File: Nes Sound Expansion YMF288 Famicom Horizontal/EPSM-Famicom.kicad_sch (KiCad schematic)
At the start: 59 parts, among them J1 CARTRIDGE_F, J2 OUT_1, J3 EPSM_ADDRESSING, J4 CONSOLE_M, J5 AudioJack4_SwitchTR1, U1 74LS174, U10 74LS257, U2 74LS174, U3 74LS139, U4 74LS132, U5 YMF288, U6 BU9480F, U7 74LS257, U8 74LS257, U9 LM358, X1 SG-8002CA

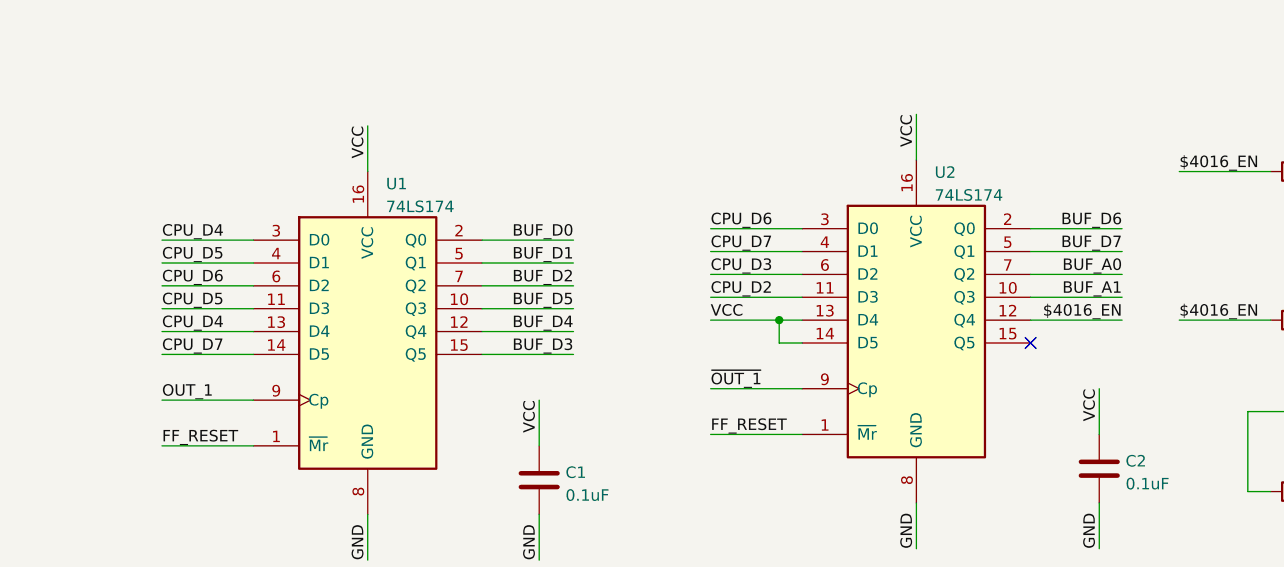
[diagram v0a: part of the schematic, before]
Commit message: Fix erroneous $4016 data latch lines
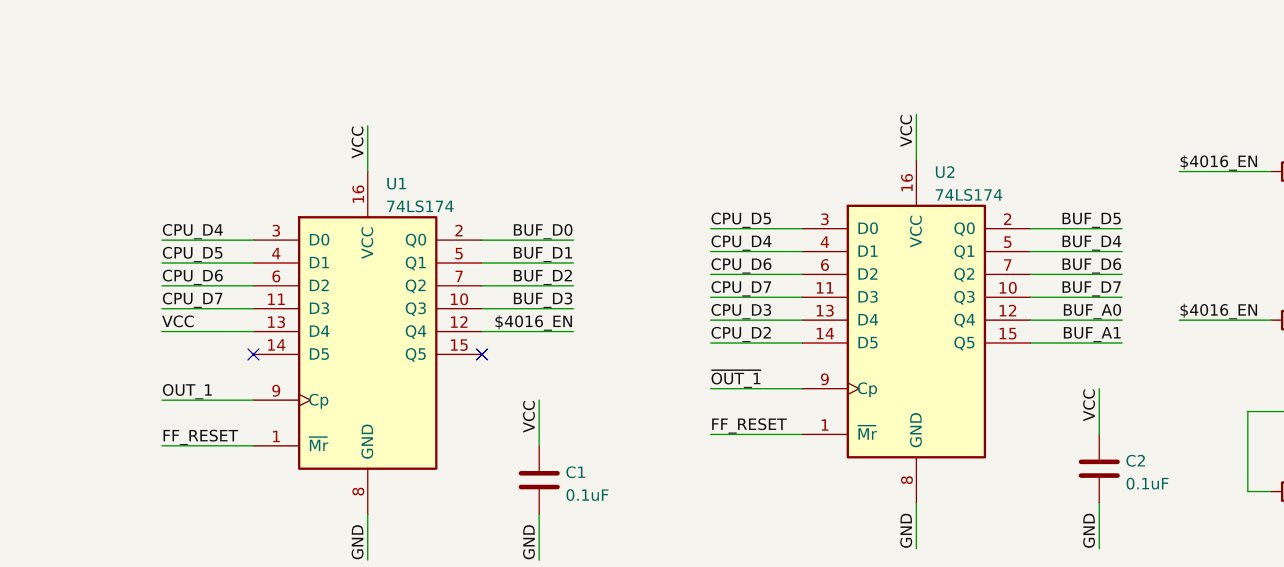
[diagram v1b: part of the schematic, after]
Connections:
- net $4016_EN: now also U1.12 (Q4); no longer U2.12 (Q4)
- net BUF_A0: now also U2.12 (Q4); no longer U2.7 (Q2)
- net BUF_A1: now also U2.15 (Q5); no longer U2.10 (Q3)
- net BUF_D3: now also U1.10 (Q3); no longer U1.15 (Q5)
- net BUF_D4: now also U2.5 (Q1); no longer U1.12 (Q4)
- net BUF_D5: now also U2.2 (Q0); no longer U1.10 (Q3)
- net BUF_D6: now also U2.7 (Q2); no longer U2.2 (Q0)
- net BUF_D7: now also U2.10 (Q3); no longer U2.5 (Q1)
- net CPU_D2: now also U2.14 (D5); no longer U2.11 (D3)
- net CPU_D3: now also U2.13 (D4); no longer U2.6 (D2)
- net CPU_D4: now also U2.4 (D1); no longer U1.13 (D4)
- net CPU_D5: now also U2.3 (D0); no longer U1.11 (D3)
- net CPU_D6: now also U2.6 (D2); no longer U2.3 (D0)
- net CPU_D7: now also U1.11 (D3), U2.11 (D3); no longer U1.14 (D5), U2.4 (D1)
- net VCC: now also U1.13 (D4); no longer U2.13 (D4), U2.14 (D5)
- no-connect marks 16 -> 17

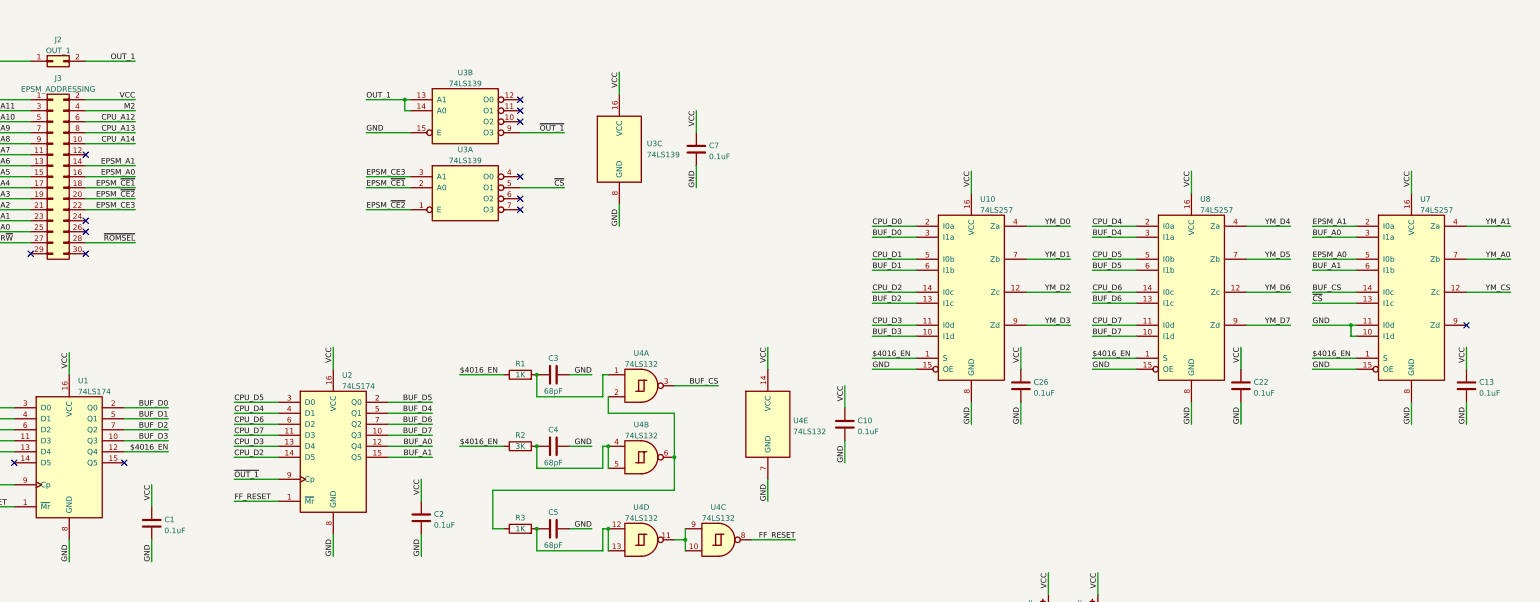
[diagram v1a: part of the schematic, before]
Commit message: Fix footprint size errors
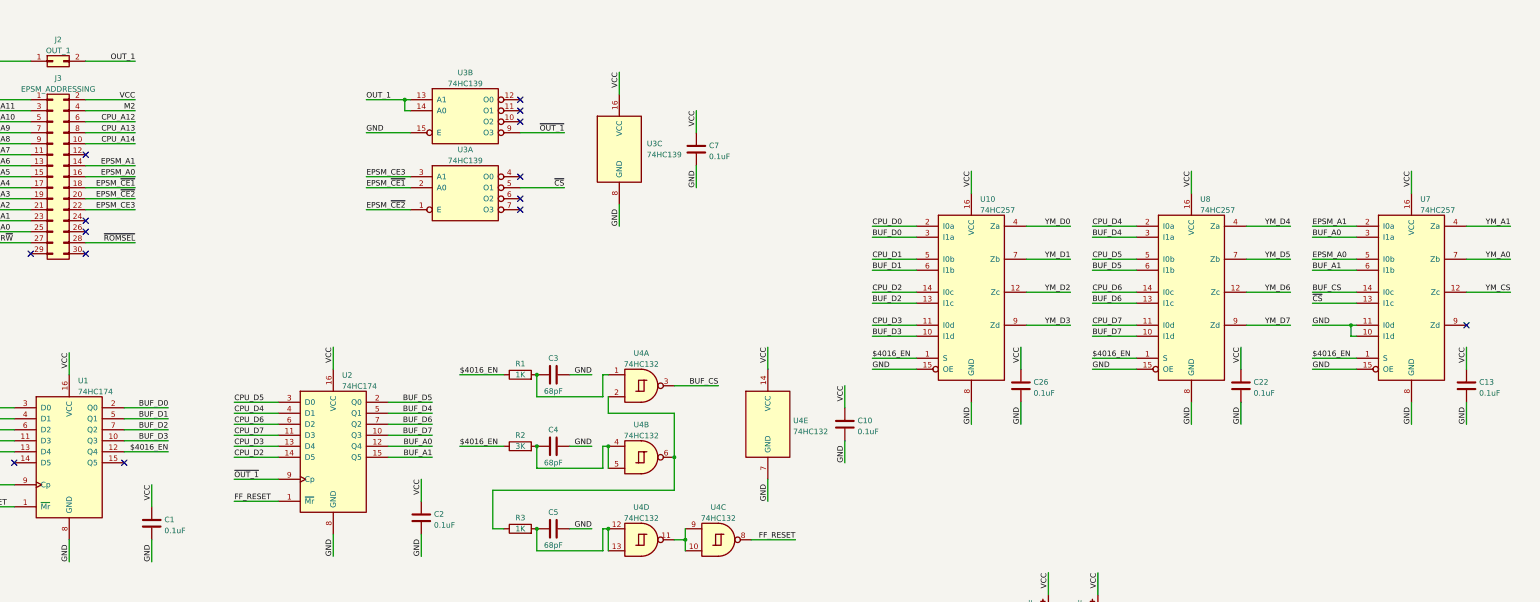
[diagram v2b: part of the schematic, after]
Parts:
- U1, U2: value 74LS174 -> 74HC174
- U10, U7, U8: value 74LS257 -> 74HC257
- U3: value 74LS139 -> 74HC139
- U4: value 74LS132 -> 74HC132
- U5: footprint EPSM-Famicom:SOP-28_7.5x12.8mm_P1.27mm -> EPSM-Famicom:SOP-28_8.4x18.1mm_P1.27mm
- U6: footprint Package_SO:SOIC-8_5.275x5.275mm_P1.27mm -> Package_SO:SOIC-8_3.9x4.9mm_P1.27mm
- X1: footprint Oscillator:Oscillator_SMD_SeikoEpson_SG8002LB-4Pin_5.0x3.2mm -> Oscillator:Oscillator_SMD_Abracon_ASV-4Pin_7.0x5.1mm
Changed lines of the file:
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@@
       (effects (font (size 1.27 1.27)) (justify left))
     )
-    (property "Footprint" "EPSM-Famicom:SOP-28_7.5x12.8mm_P1.27mm" (id 2) (at 195.58 81.28 0)
-      (effects (font (size 1.27 1.27)) hide)
-    )
-    (property "Datasheet" "" (id 3) (at 195.58 81.28 0)
+    (property "Footprint" "EPSM-Famicom:SOP-28_8.4x18.1mm_P1.27mm" (id 2) (at 195.58 81.28 0)
+      (effects (font (size 1.27 1.27)) hide)
+    )
+    (property "Datasheet" "https://www.quarter-dev.info/archives/yamaha/YMF288.pdf" (id 3) (at 195.58 81.28 0)
       (effects (font (size 1.27 1.27)) hide)
     )
@@
       (effects (font (size 1.27 1.27)) (justify left))
     )
-    (property "Value" "74LS257" (id 1) (at 258.5594 175.3671 0)
+    (property "Value" "74HC257" (id 1) (at 258.5594 175.3671 0)
       (effects (font (size 1.27 1.27)) (justify left))
     )
@@
       (effects (font (size 1.27 1.27)) (justify left))
     )
-    (property "Value" "74LS174" (id 1) (at 111.2394 216.0071 0)
+    (property "Value" "74HC174" (id 1) (at 111.2394 216.0071 0)
       (effects (font (size 1.27 1.27)) (justify left))
     )
@@
       (effects (font (size 1.27 1.27)) (justify left))
     )
-    (property "Value" "74LS257" (id 1) (at 309.3594 175.3671 0)
+    (property "Value" "74HC257" (id 1) (at 309.3594 175.3671 0)
       (effects (font (size 1.27 1.27)) (justify left))
     )
@@
     (in_bom yes) (on_board yes)
     (property "Reference" "U4" (id 0) (at 180.34 243.9502 0))
-    (property "Value" "74LS132" (id 1) (at 180.34 246.4871 0))
+    (property "Value" "74HC132" (id 1) (at 180.34 246.4871 0))
     (property "Footprint" "Package_SO:SOIC-14_3.9x8.7mm_P1.27mm" (id 2) (at 180.34 251.46 0)
       (effects (font (size 1.27 1.27)) hide)
@@
       (effects (font (size 1.27 1.27)) (justify left))
     )
-    (property "Footprint" "Oscillator:Oscillator_SMD_SeikoEpson_SG8002LB-4Pin_5.0x3.2mm" (id 2) (at 226.06 55.88 0)
+    (property "Footprint" "Oscillator:Oscillator_SMD_Abracon_ASV-4Pin_7.0x5.1mm" (id 2) (at 226.06 55.88 0)
       (effects (font (size 1.27 1.27)) hide)
     )
@@
     (in_bom yes) (on_board yes) (fields_autoplaced)
     (property "Reference" "U3" (id 0) (at 139.7 161.4002 0))
-    (property "Value" "74LS139" (id 1) (at 139.7 163.9371 0))
+    (property "Value" "74HC139" (id 1) (at 139.7 163.9371 0))
     (property "Footprint" "Package_SO:SOIC-16_3.9x9.9mm_P1.27mm" (id 2) (at 139.7 170.18 0)
       (effects (font (size 1.27 1.27)) hide)
@@
     (in_bom yes) (on_board yes) (fields_autoplaced)
     (property "Reference" "U4" (id 0) (at 180.34 224.9002 0))
-    (property "Value" "74LS132" (id 1) (at 180.34 227.4371 0))
+    (property "Value" "74HC132" (id 1) (at 180.34 227.4371 0))
     (property "Footprint" "Package_SO:SOIC-14_3.9x8.7mm_P1.27mm" (id 2) (at 180.34 232.41 0)
       (effects (font (size 1.27 1.27)) hide)
@@
       (effects (font (size 1.27 1.27)) (justify left))
     )
-    (property "Value" "74LS132" (id 1) (at 215.392 226.4922 0)
+    (property "Value" "74HC132" (id 1) (at 215.392 226.4922 0)
       (effects (font (size 1.27 1.27)) (justify left))
     )
@@
     (in_bom yes) (on_board yes) (fields_autoplaced)
     (property "Reference" "U4" (id 0) (at 180.34 208.3902 0))
-    (property "Value" "74LS132" (id 1) (at 180.34 210.9271 0))
+    (property "Value" "74HC132" (id 1) (at 180.34 210.9271 0))
     (property "Footprint" "Package_SO:SOIC-14_3.9x8.7mm_P1.27mm" (id 2) (at 180.34 215.9 0)
       (effects (font (size 1.27 1.27)) hide)
@@
       (effects (font (size 1.27 1.27)) (justify left))
     )
-    (property "Value" "74LS257" (id 1) (at 360.1594 175.3671 0)
+    (property "Value" "74HC257" (id 1) (at 360.1594 175.3671 0)
       (effects (font (size 1.27 1.27)) (justify left))
     )
@@
     (in_bom yes) (on_board yes) (fields_autoplaced)
     (property "Reference" "U3" (id 0) (at 139.7 143.6202 0))
-    (property "Value" "74LS139" (id 1) (at 139.7 146.1571 0))
+    (property "Value" "74HC139" (id 1) (at 139.7 146.1571 0))
     (property "Footprint" "Package_SO:SOIC-16_3.9x9.9mm_P1.27mm" (id 2) (at 139.7 152.4 0)
       (effects (font (size 1.27 1.27)) hide)
@@
     (in_bom yes) (on_board yes) (fields_autoplaced)
     (property "Reference" "U4" (id 0) (at 198.12 243.9502 0))
-    (property "Value" "74LS132" (id 1) (at 198.12 246.4871 0))
+    (property "Value" "74HC132" (id 1) (at 198.12 246.4871 0))
     (property "Footprint" "Package_SO:SOIC-14_3.9x8.7mm_P1.27mm" (id 2) (at 198.12 251.46 0)
       (effects (font (size 1.27 1.27)) hide)
@@
       (effects (font (size 1.27 1.27)) (justify left))
     )
-    (property "Value" "74LS139" (id 1) (at 181.61 162.56 0)
+    (property "Value" "74HC139" (id 1) (at 181.61 162.56 0)
       (effects (font (size 1.27 1.27)) (justify left))
     )
@@
       (effects (font (size 1.27 1.27)) (justify left))
     )
-    (property "Footprint" "Package_SO:SOIC-8_5.275x5.275mm_P1.27mm" (id 2) (at 233.68 74.93 0)
+    (property "Footprint" "Package_SO:SOIC-8_3.9x4.9mm_P1.27mm" (id 2) (at 233.68 74.93 0)
       (effects (font (size 1.27 1.27)) hide)
     )
@@
       (effects (font (size 1.27 1.27)) (justify left))
     )
-    (property "Value" "74LS174" (id 1) (at 50.2794 217.2771 0)
+    (property "Value" "74HC174" (id 1) (at 50.2794 217.2771 0)
       (effects (font (size 1.27 1.27)) (justify left))
     )
@@
     )
     (path "/ffa9b3d0-5a2b-4008-a1d1-ba0783fbcd78"
-      (reference "U1") (unit 1) (value "74LS174") (footprint "Package_SO:SOIC-16_3.9x9.9mm_P1.27mm")
+      (reference "U1") (unit 1) (value "74HC174") (footprint "Package_SO:SOIC-16_3.9x9.9mm_P1.27mm")
     )
     (path "/0a512736-9db6-4093-98c5-8298b2002bd9"
-      (reference "U2") (unit 1) (value "74LS174") (footprint "Package_SO:SOIC-16_3.9x9.9mm_P1.27mm")
+      (reference "U2") (unit 1) (value "74HC174") (footprint "Package_SO:SOIC-16_3.9x9.9mm_P1.27mm")
     )
     (path "/48d1e52a-2236-4c12-94d5-ffccc100ea49"
-      (reference "U3") (unit 1) (value "74LS139") (footprint "Package_SO:SOIC-16_3.9x9.9mm_P1.27mm")
+      (reference "U3") (unit 1) (value "74HC139") (footprint "Package_SO:SOIC-16_3.9x9.9mm_P1.27mm")
     )
     (path "/94ff7ccf-1795-4c28-b581-f2ea7c835610"
-      (reference "U3") (unit 2) (value "74LS139") (footprint "Package_SO:SOIC-16_3.9x9.9mm_P1.27mm")
+      (reference "U3") (unit 2) (value "74HC139") (footprint "Package_SO:SOIC-16_3.9x9.9mm_P1.27mm")
     )
     (path "/c0c18a2a-6376-4fa0-9928-c3b0ce3e0e91"
-      (reference "U3") (unit 3) (value "74LS139") (footprint "Package_SO:SOIC-16_3.9x9.9mm_P1.27mm")
+      (reference "U3") (unit 3) (value "74HC139") (footprint "Package_SO:SOIC-16_3.9x9.9mm_P1.27mm")
     )
     (path "/83ed3325-163c-4afa-93c5-49baeb4cd081"
-      (reference "U4") (unit 1) (value "74LS132") (footprint "Package_SO:SOIC-14_3.9x8.7mm_P1.27mm")
+      (reference "U4") (unit 1) (value "74HC132") (footprint "Package_SO:SOIC-14_3.9x8.7mm_P1.27mm")
     )
     (path "/599fbcfe-5e39-4f5e-8245-7a38ebea64d1"
-      (reference "U4") (unit 2) (value "74LS132") (footprint "Package_SO:SOIC-14_3.9x8.7mm_P1.27mm")
+      (reference "U4") (unit 2) (value "74HC132") (footprint "Package_SO:SOIC-14_3.9x8.7mm_P1.27mm")
     )
     (path "/a010cd21-0c47-4838-97cf-f6952c9f247c"
-      (reference "U4") (unit 3) (value "74LS132") (footprint "Package_SO:SOIC-14_3.9x8.7mm_P1.27mm")
+      (reference "U4") (unit 3) (value "74HC132") (footprint "Package_SO:SOIC-14_3.9x8.7mm_P1.27mm")
     )
     (path "/2d006010-ba6c-4126-adf6-9df43d863282"
-      (reference "U4") (unit 4) (value "74LS132") (footprint "Package_SO:SOIC-14_3.9x8.7mm_P1.27mm")
+      (reference "U4") (unit 4) (value "74HC132") (footprint "Package_SO:SOIC-14_3.9x8.7mm_P1.27mm")
     )
     (path "/789ef0a4-200d-4a4a-b78e-3e6610a4c3b8"
-      (reference "U4") (unit 5) (value "74LS132") (footprint "Package_SO:SOIC-14_3.9x8.7mm_P1.27mm")
+      (reference "U4") (unit 5) (value "74HC132") (footprint "Package_SO:SOIC-14_3.9x8.7mm_P1.27mm")
     )
     (path "/04721b2a-b8fe-4628-b3cc-831c2dbc8b4f"
-      (reference "U5") (unit 1) (value "YMF288") (footprint "EPSM-Famicom:SOP-28_7.5x12.8mm_P1.27mm")
+      (reference "U5") (unit 1) (value "YMF288") (footprint "EPSM-Famicom:SOP-28_8.4x18.1mm_P1.27mm")
     )
     (path "/d02f9b5f-57b8-4b22-ba74-372e25af5469"
-      (reference "U6") (unit 1) (value "BU9480F") (footprint "Package_SO:SOIC-8_5.275x5.275mm_P1.27mm")
+      (reference "U6") (unit 1) (value "BU9480F") (footprint "Package_SO:SOIC-8_3.9x4.9mm_P1.27mm")
     )
     (path "/91bb666c-cdad-4b85-b6b9-1567d0f51104"
-      (reference "U7") (unit 1) (value "74LS257") (footprint "Package_SO:SOIC-16_3.9x9.9mm_P1.27mm")
+      (reference "U7") (unit 1) (value "74HC257") (footprint "Package_SO:SOIC-16_3.9x9.9mm_P1.27mm")
     )
     (path "/13e2216a-5685-44fb-b37b-e3377d494a4d"
-      (reference "U8") (unit 1) (value "74LS257") (footprint "Package_SO:SOIC-16_3.9x9.9mm_P1.27mm")
+      (reference "U8") (unit 1) (value "74HC257") (footprint "Package_SO:SOIC-16_3.9x9.9mm_P1.27mm")
     )
     (path "/387d75e5-30ff-4e24-b0ee-c5bf67a456b6"
@@
     )
     (path "/07e9be1b-d34d-4a14-ad60-a9f8f1ba9a04"
-      (reference "U10") (unit 1) (value "74LS257") (footprint "Package_SO:SOIC-16_3.9x9.9mm_P1.27mm")
+      (reference "U10") (unit 1) (value "74HC257") (footprint "Package_SO:SOIC-16_3.9x9.9mm_P1.27mm")
     )
     (path "/487fe2b3-0e38-4935-9823-96c09d72da99"
-      (reference "X1") (unit 1) (value "SG-8002CA") (footprint "Oscillator:Oscillator_SMD_SeikoEpson_SG8002LB-4Pin_5.0x3.2mm")
-    )
-  )
+      (reference "X1") (unit 1) (value "SG-8002CA") (footprint "Oscillator:Oscillator_SMD_Abracon_ASV-4Pin_7.0x5.1mm")
+    )
+  )

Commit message: Remove daughterboard connector; use two layers
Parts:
- removed C14, C15: 100uF, Capacitor_THT:CP_Radial_D5.0mm_P2.50mm, symbol Device:C_Polarized
- removed J2: OUT_1, Connector_PinHeader_2.54mm:PinHeader_1x02_P2.54mm_Vertical, symbol Connector_Generic:Conn_02x01
- removed J3: EPSM_ADDRESSING, Connector_PinSocket_2.54mm:PinSocket_2x15_P2.54mm_Vertical_SMD, symbol Connector_Generic:Conn_02x15_Odd_Even
- added C1, C10, C21, C30, C4: 0.1uF, Capacitor_SMD:C_0805_2012Metric_Pad1.18x1.45mm_HandSolder, symbol Device:C
- added C16, C18: 100uF, Capacitor_SMD:CP_Elec_6.3x5.4, symbol Device:C_Polarized
- added U1, U5, U6: 74HC688, Package_SO:SOIC-20W_7.5x12.8mm_P1.27mm, symbol 74xx:74HC688
- added U10: 74HC132, Package_SO:SOIC-14_3.9x8.7mm_P1.27mm, symbol 74xx:74LS132
- added U14: 74LVC1G373, Package_TO_SOT_SMD:SOT-23-6, symbol 74xGxx:74LVC1G373
- renumbered C8 to C11, C10 to C12, C9 to C13, C11 to C14, C12 to C15, C26 to C17, C16 to C19, C1 to C2, C17 to C20, C18 to C22, C19 to C23, C20 to C24, C21 to C25, C22 to C26, C23 to C27, C24 to C28, C25 to C29, C7 to C3, C13 to C31, C2 to C5, C3 to C6, C4 to C7, C5 to C8, C6 to C9, J4 to J2, J5 to J3, U10 to U11, U8 to U12, U9 to U13, U7 to U15, U3 to U2, U1 to U3, U2 to U4, U4 to U7, U5 to U8, U6 to U9
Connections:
- net EPSM_CE3 is gone; now on net VCC: U2.3 (A1)
- net EPSM_~{CE1} is gone; now on net GND: U2.2 (A0)
- net $4016_EN: now also U3.7 (Q2); no longer U3.12 (Q4)
- net BUF_A0: now also U4.7 (Q2); no longer U4.12 (Q4)
- net BUF_A1: now also U15.13 (I1c), U4.10 (Q3); no longer U15.6 (I1b), U4.15 (Q5)
- net BUF_CS: now also U15.5 (I0b); no longer U15.14 (I0c)
- net BUF_D0: now also U3.5 (Q1); no longer U3.2 (Q0)
- net BUF_D1: now also U11.13 (I1c), U3.12 (Q4); no longer U11.6 (I1b), U3.5 (Q1)
- net BUF_D2: now also U11.6 (I1b), U3.2 (Q0); no longer U11.13 (I1c), U3.7 (Q2)
- net BUF_D3: now also U3.15 (Q5); no longer U3.10 (Q3)
- net BUF_D5: now also U12.13 (I1c), U4.12 (Q4); no longer U12.6 (I1b), U4.2 (Q0)
- net BUF_D6: now also U12.6 (I1b), U4.2 (Q0); no longer U12.13 (I1c), U4.7 (Q2)
- net BUF_D7: now also U4.15 (Q5); no longer U4.10 (Q3)
- net CPU_A0: now also U6.13 (P5)
- net CPU_A1: now also U6.15 (P6)
- net CPU_A10: now also U1.4 (P1)
- net CPU_A11: now also U1.8 (P3)
- net CPU_A12: now also U1.6 (P2)
- net CPU_A13: now also U1.2 (P0)
- net CPU_A14: now also U1.15 (P6)
- net CPU_A2: now also U5.15 (P6), U6.17 (P7)
- net CPU_A3: now also U5.17 (P7), U6.2 (P0)
- net CPU_A4: now also U5.8 (P3), U6.4 (P1)
- net CPU_A5: now also U5.6 (P2), U6.6 (P2)
- net CPU_A6: now also U5.4 (P1), U6.8 (P3)
- net CPU_A7: now also U1.11 (P4)
- net CPU_A8: now also U1.13 (P5)
- net CPU_A9: now also U1.17 (P7)
- net CPU_D1: now also U11.14 (I0c), U14.3 (D); no longer U11.5 (I0b)
- net CPU_D2: now also U11.5 (I0b), U4.11 (D3); no longer U11.14 (I0c), U4.14 (D5)
- net CPU_D3: now also U4.6 (D2); no longer U4.13 (D4)
- net CPU_D4: now also U3.4 (D1); no longer U3.3 (D0)
- net CPU_D5: now also U12.14 (I0c), U3.13 (D4), U4.13 (D4); no longer U12.5 (I0b), U3.4 (D1), U4.3 (D0)
- net CPU_D6: now also U12.5 (I0b), U3.3 (D0), U4.3 (D0); no longer U12.14 (I0c), U3.6 (D2), U4.6 (D2)
- net CPU_D7: now also U3.14 (D5), U4.14 (D5); no longer U3.11 (D3), U4.11 (D3)
- net CPU_R~{W}: now also U10.1, U10.2, U5.11 (P4)
- net EPSM_A0: now also U15.14 (I0c); no longer U15.5 (I0b)
- net GND: now also C1.1, C10.1, C16.2, C18.2, C21.1, C30.1, C4.1, U1.1 (G), U1.10 (GND), U1.12 (R4), U1.14 (R5), U1.18 (R7), U1.3 (R0), U1.5 (R1), U1.7 (R2), U1.9 (R3), U10.7 (GND), U14.2 (GND), U14.6 (~{OE}), U5.10 (GND), U5.12 (R4), U5.5 (R1), U5.7 (R2), U6.10 (GND), U6.14 (R5), U6.3 (R0), U6.7 (R2), U6.9 (R3)
- net M2: now also U5.2 (P0)
- net OUT_1: now also U14.4 (Q)
- net VCC: now also U3.11 (D3), U3.6 (D2), C1.2, C10.2, C16.1, C18.1, C21.2, C30.2, C4.2, U1.16 (R6), U1.20 (VCC), U10.14 (VCC), U14.5 (VCC), U5.14 (R5), U5.16 (R6), U5.18 (R7), U5.20 (VCC), U5.3 (R0), U5.9 (R3), U6.12 (R4), U6.16 (R6), U6.18 (R7), U6.20 (VCC), U6.5 (R1); no longer U3.13 (D4)
- net YM_A0: now also U15.12 (Zc); no longer U15.7 (Zb)
- net YM_CS: now also U15.7 (Zb); no longer U15.12 (Zc)
- net YM_D1: now also U11.12 (Zc); no longer U11.7 (Zb)
- net YM_D2: now also U11.7 (Zb); no longer U11.12 (Zc)
- net YM_D5: now also U12.12 (Zc); no longer U12.7 (Zb)
- net YM_D6: now also U12.7 (Zb); no longer U12.12 (Zc)
- net ~{CS}: now also U15.6 (I1b); no longer U15.13 (I1c)
- net ~{ROMSEL}: now also U5.13 (P5), U6.11 (P4)
- net at U7.12, U7.13: no longer C8.1, R3.2
- net EPSM_~{CE2} renamed $401x_~{CE}
- net $401x_~{CE}: now also U5.19 (P=R)
- new net: U10.10, U10.11, U10.9
- new net: C8.1, R3.2
- new net: U10.12, U10.3
- new net: U10.13, U10.6
- new net $4016_~{CE}: U10.4, U10.5, U6.19 (P=R)
- new net $40xx_~{CE}: U1.19 (P=R), U5.1 (G), U6.1 (G)
- new net OUT_1_CE: U10.8, U14.1 (LE)
- no-connect marks 17 -> 11
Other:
- note added: "$4016 W CPU_A0 = 0 CPU_A1 = 1 CPU_A2 = 1 CPU_A3 = 0 CPU_A4 = 1 CPU_A5 = 0 CPU_A6 = 0 ~{ROMSEL} = 1"
- note added: "$401C-F W CPU_A2 = 1 CPU_A3 = 1 CPU_A4 = 1 CPU_A5 = 0 CPU_A6 = 0 ~{ROMSEL} = 1 CPU_R~{W} = 0 M2 = 1"
- note added: "CPU_A7 = 0 CPU_A8 = 0 CPU_A9 = 0 CPU_A10 = 0 CPU_A11 = 0 CPU_A12 = 0 CPU_A13 = 0 CPU_A14 = 1"
- moved on the sheet: C11, C12, C13, C14, C15, C17, C19, C2, C20, C22, C23, C24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
